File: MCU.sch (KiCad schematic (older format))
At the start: 33 parts, among them J1 USB_OTG, U1 STM32F103R4T6, Y1 8.000MHz

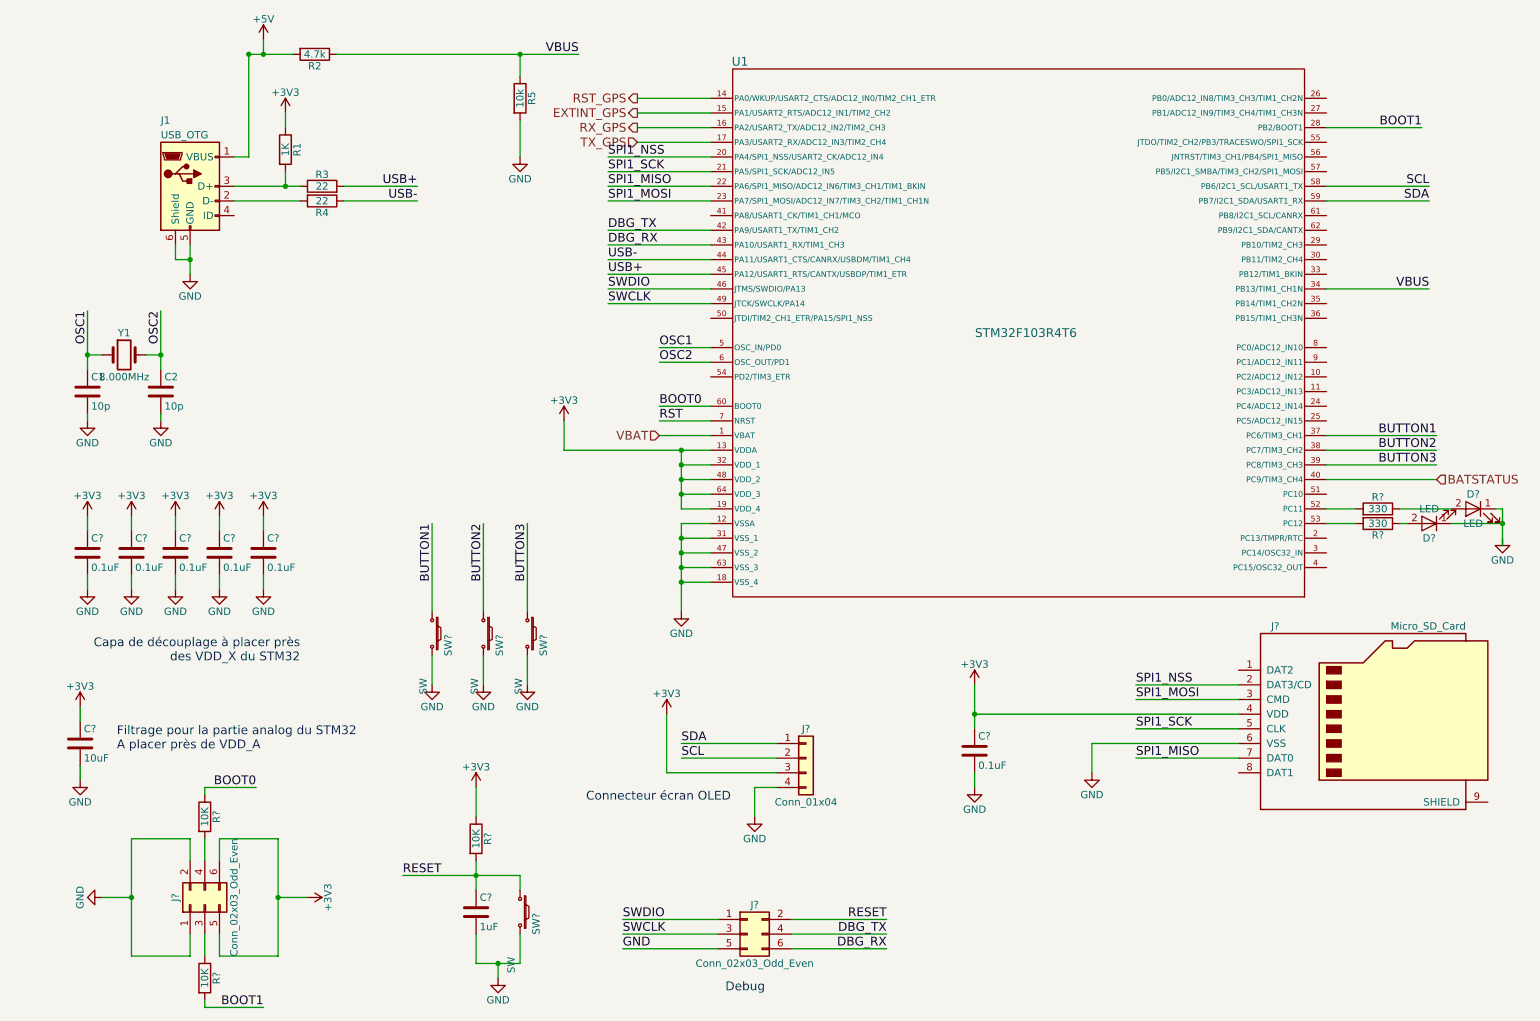
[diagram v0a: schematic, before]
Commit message: Improve battery as power source
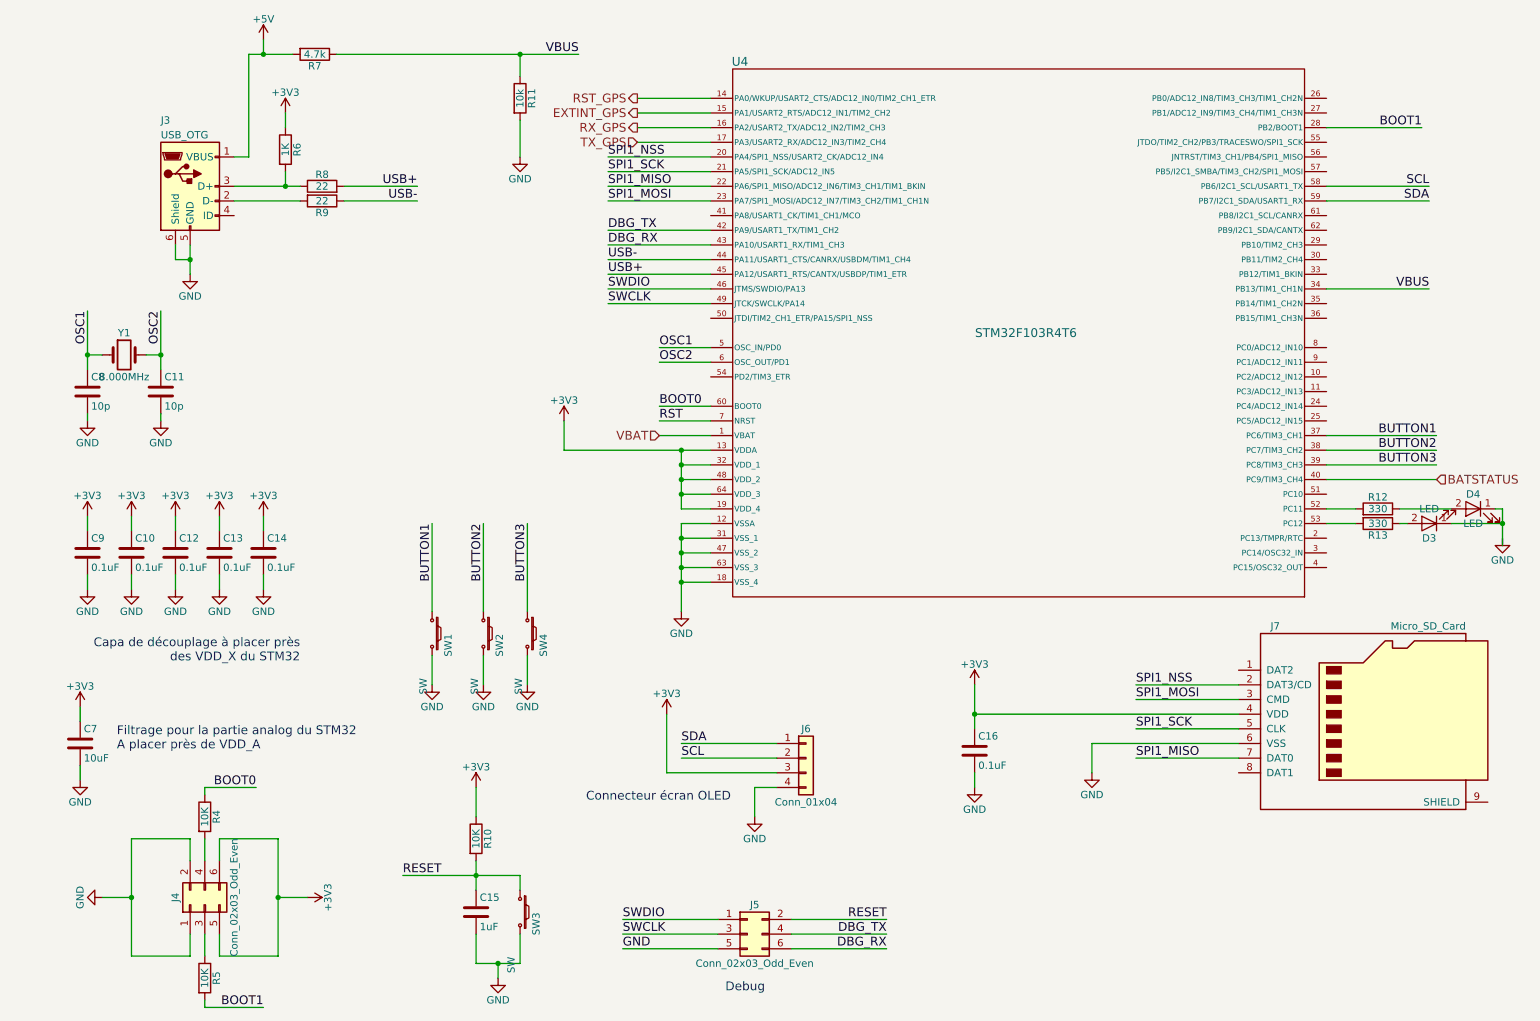
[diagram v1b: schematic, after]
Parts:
- gave numbers to parts that had none: 23
- renumbered C2 to C11, C1 to C8, J1 to J3, R5 to R11, R1 to R6, R2 to R7, R3 to R8, R4 to R9, U1 to U4
